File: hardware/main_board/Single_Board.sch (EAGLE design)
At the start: 54 parts, among them J2 U.FL, J3 AVR_SPI_PROG_3X2NS, Q1 2N7002, Q2 AO3400A, Q3 S9015, U1 INA199B1DCKR, U2 MCP1703T-3302E/CB, U4 W25X40CLUXIG_TR, U5 ATMEGA328PB-AU, X1 32.768KHZ-FC-135, X2 B2B-PH-K-S, X3 B2B-XH-2, X4 BM02B-SRSS-TB, X5 BM02B-SRSS-TB

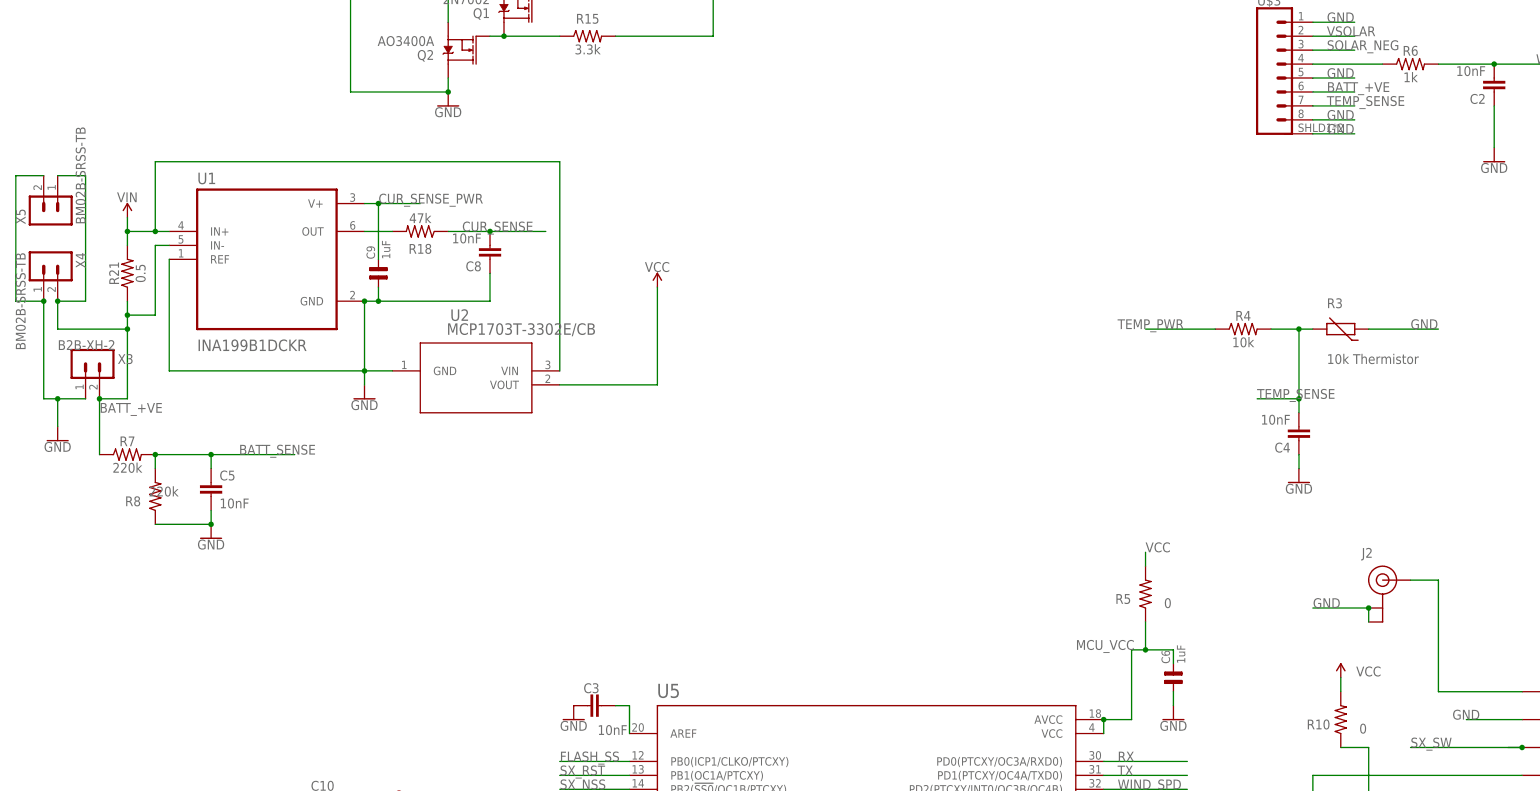
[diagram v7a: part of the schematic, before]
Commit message: Board improvements: Fixed 8P8C jack footprint. Better antenna trace impedance. Added anti-static resistor to antenna
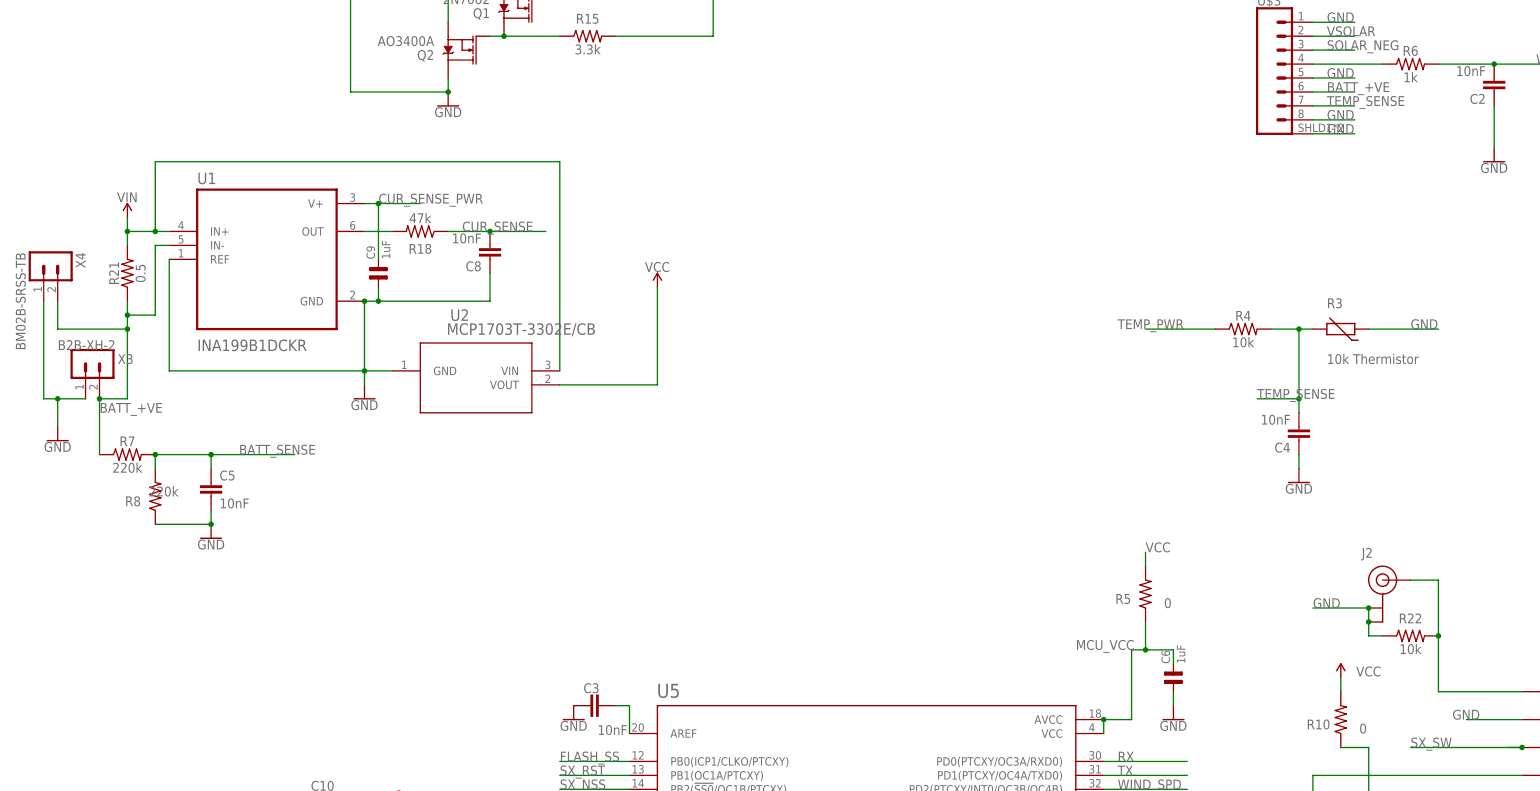
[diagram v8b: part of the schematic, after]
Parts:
- removed X5: BM02B-SRSS-TB, main_board:BM02B-SRSS-TB
- added R22: 10k, SparkFun-Resistors:RESISTOR0805
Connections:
- net ANT: now also R22.2
- net BATT_+VE: no longer X5.1
- net GND: now also R22.1; no longer X5.2
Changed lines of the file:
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@@
 <grid distance="0.1" unitdist="inch" unit="inch" style="lines" multiple="1" display="no" altdistance="0.01" altunitdist="inch" altunit="inch"/>
 <layers>
-<layer number="1" name="Top" color="4" fill="1" visible="yes" active="no"/>
-<layer number="16" name="Bottom" color="1" fill="1" visible="yes" active="no"/>
-<layer number="17" name="Pads" color="2" fill="1" visible="yes" active="no"/>
-<layer number="18" name="Vias" color="2" fill="1" visible="yes" active="no"/>
-<layer number="19" name="Unrouted" color="6" fill="1" visible="yes" active="no"/>
-<layer number="20" name="Dimension" color="36" fill="1" visible="yes" active="no"/>
-<layer number="21" name="tPlace" color="7" fill="1" visible="yes" active="no"/>
-<layer number="22" name="bPlace" color="7" fill="1" visible="yes" active="no"/>
-<layer number="23" name="tOrigins" color="15" fill="1" visible="yes" active="no"/>
-<layer number="24" name="bOrigins" color="15" fill="1" visible="yes" active="no"/>
-<layer number="25" name="tNames" color="7" fill="1" visible="yes" active="no"/>
-<layer number="26" name="bNames" color="7" fill="1" visible="yes" active="no"/>
-<layer number="27" name="tValues" color="7" fill="1" visible="yes" active="no"/>
-<layer number="28" name="bValues" color="7" fill="1" visible="yes" active="no"/>
+<layer number="1" name="Top" color="4" fill="1" visible="no" active="no"/>
+<layer number="16" name="Bottom" color="1" fill="1" visible="no" active="no"/>
+<layer number="17" name="Pads" color="2" fill="1" visible="no" active="no"/>
+<layer number="18" name="Vias" color="2" fill="1" visible="no" active="no"/>
+<layer number="19" name="Unrouted" color="6" fill="1" visible="no" active="no"/>
+<layer number="20" name="Dimension" color="36" fill="1" visible="no" active="no"/>
+<layer number="21" name="tPlace" color="7" fill="1" visible="no" active="no"/>
+<layer number="22" name="bPlace" color="7" fill="1" visible="no" active="no"/>
+<layer number="23" name="tOrigins" color="15" fill="1" visible="no" active="no"/>
+<layer number="24" name="bOrigins" color="15" fill="1" visible="no" active="no"/>
+<layer number="25" name="tNames" color="7" fill="1" visible="no" active="no"/>
+<layer number="26" name="bNames" color="7" fill="1" visible="no" active="no"/>
+<layer number="27" name="tValues" color="7" fill="1" visible="no" active="no"/>
+<layer number="28" name="bValues" color="7" fill="1" visible="no" active="no"/>
 <layer number="29" name="tStop" color="7" fill="3" visible="no" active="no"/>
 <layer number="30" name="bStop" color="7" fill="6" visible="no" active="no"/>
@@
 <layer number="35" name="tGlue" color="7" fill="4" visible="no" active="no"/>
 <layer number="36" name="bGlue" color="7" fill="5" visible="no" active="no"/>
-<layer number="37" name="tTest" color="7" fill="1" visible="yes" active="no"/>
-<layer number="38" name="bTest" color="7" fill="1" visible="yes" active="no"/>
+<layer number="37" name="tTest" color="7" fill="1" visible="no" active="no"/>
+<layer number="38" name="bTest" color="7" fill="1" visible="no" active="no"/>
 <layer number="39" name="tKeepout" color="4" fill="11" visible="no" active="no"/>
 <layer number="40" name="bKeepout" color="1" fill="11" visible="no" active="no"/>
@@
 <layer number="44" name="Drills" color="7" fill="1" visible="no" active="no"/>
 <layer number="45" name="Holes" color="7" fill="1" visible="no" active="no"/>
-<layer number="46" name="Milling" color="3" fill="1" visible="yes" active="no"/>
-<layer number="47" name="Measures" color="7" fill="1" visible="yes" active="no"/>
-<layer number="48" name="Document" color="7" fill="1" visible="yes" active="no"/>
-<layer number="49" name="Reference" color="7" fill="1" visible="yes" active="no"/>
-<layer number="50" name="dxf" color="7" fill="1" visible="yes" active="no"/>
-<layer number="51" name="tDocu" color="7" fill="1" visible="yes" active="no"/>
-<layer number="52" name="bDocu" color="7" fill="1" visible="yes" active="no"/>
-<layer number="53" name="tGND_GNDA" color="7" fill="9" visible="yes" active="no"/>
-<layer number="54" name="bGND_GNDA" color="1" fill="9" visible="yes" active="no"/>
-<layer number="56" name="wert" color="7" fill="1" visible="yes" active="no"/>
-<layer number="57" name="tCAD" color="7" fill="1" visible="yes" active="no"/>
-<layer number="59" name="tCarbon" color="7" fill="1" visible="yes" active="no"/>
-<layer number="60" name="bCarbon" color="7" fill="1" visible="yes" active="no"/>
+<layer number="46" name="Milling" color="3" fill="1" visible="no" active="no"/>
+<layer number="47" name="Measures" color="7" fill="1" visible="no" active="no"/>
+<layer number="48" name="Document" color="7" fill="1" visible="no" active="no"/>
+<layer number="49" name="Reference" color="7" fill="1" visible="no" active="no"/>
+<layer number="50" name="dxf" color="7" fill="1" visible="no" active="no"/>
+<layer number="51" name="tDocu" color="7" fill="1" visible="no" active="no"/>
+<layer number="52" name="bDocu" color="7" fill="1" visible="no" active="no"/>
+<layer number="53" name="tGND_GNDA" color="7" fill="9" visible="no" active="no"/>
+<layer number="54" name="bGND_GNDA" color="1" fill="9" visible="no" active="no"/>
+<layer number="56" name="wert" color="7" fill="1" visible="no" active="no"/>
+<layer number="57" name="tCAD" color="7" fill="1" visible="no" active="no"/>
+<layer number="59" name="tCarbon" color="7" fill="1" visible="no" active="no"/>
+<layer number="60" name="bCarbon" color="7" fill="1" visible="no" active="no"/>
 <layer number="88" name="SimResults" color="9" fill="1" visible="yes" active="yes"/>
 <layer number="89" name="SimProbes" color="9" fill="1" visible="yes" active="yes"/>
@@
 <part name="U4" library="main_board" deviceset="W25X40CLUXIG_TR" device=""/>
 <part name="X4" library="main_board" deviceset="BM02B-SRSS" device="-TB"/>
-<part name="X5" library="main_board" deviceset="BM02B-SRSS" device="-TB"/>
 <part name="R20" library="SparkFun-Resistors" library_urn="urn:adsk.eagle:library:532" deviceset="RESISTOR" device="0805" package3d_urn="urn:adsk.eagle:package:39651/1" value="10k"/>
+<part name="R22" library="SparkFun-Resistors" library_urn="urn:adsk.eagle:library:532" deviceset="RESISTOR" device="0805" package3d_urn="urn:adsk.eagle:package:39651/1" value="10k"/>
 </parts>
 <sheets>
@@
 <attribute name="NAME" x="-136.398" y="-13.97" size="1.778" layer="95" rot="R270"/>
 </instance>
-<instance part="X5" gate="G$1" x="-142.24" y="-7.62" smashed="yes" rot="R90">
-<attribute name="VALUE" x="-134.62" y="-8.89" size="1.778" layer="96" rot="R90"/>
-<attribute name="NAME" x="-145.542" y="-8.89" size="1.778" layer="95" rot="R90"/>
-</instance>
 <instance part="R20" gate="G$1" x="-33.02" y="40.64" smashed="yes">
 <attribute name="NAME" x="-33.02" y="44.704" size="1.778" layer="95" font="vector" rot="R180" align="bottom-center"/>
 <attribute name="VALUE" x="-33.02" y="39.116" size="1.778" layer="96" font="vector" align="top-center"/>
+</instance>
+<instance part="R22" gate="G$1" x="106.68" y="-83.82" smashed="yes">
+<attribute name="NAME" x="106.68" y="-79.756" size="1.778" layer="95" font="vector" rot="R180" align="bottom-center"/>
+<attribute name="VALUE" x="106.68" y="-85.344" size="1.778" layer="96" font="vector" align="top-center"/>
 </instance>
 </instances>
@@
 <wire x1="-142.24" y1="-40.64" x2="-139.7" y2="-40.64" width="0.1524" layer="91"/>
 <junction x="-139.7" y="-40.64"/>
-<wire x1="-142.24" y1="-22.86" x2="-147.32" y2="-22.86" width="0.1524" layer="91"/>
-<junction x="-142.24" y="-22.86"/>
-<wire x1="-147.32" y1="-22.86" x2="-147.32" y2="0" width="0.1524" layer="91"/>
-<pinref part="X5" gate="G$1" pin="2"/>
-<wire x1="-147.32" y1="0" x2="-142.24" y2="0" width="0.1524" layer="91"/>
 </segment>
 <segment>
@@
 <junction x="99.06" y="-78.74"/>
 <label x="88.9" y="-78.74" size="1.778" layer="95"/>
+<pinref part="R22" gate="G$1" pin="1"/>
+<wire x1="101.6" y1="-83.82" x2="99.06" y2="-83.82" width="0.1524" layer="91"/>
+<wire x1="99.06" y1="-83.82" x2="99.06" y2="-81.28" width="0.1524" layer="91"/>
+<junction x="99.06" y="-81.28"/>
 </segment>
 <segment>
@@
 <net name="ANT" class="0">
 <segment>
-<wire x1="111.76" y1="-93.98" x2="111.76" y2="-73.66" width="0.1524" layer="91"/>
+<wire x1="111.76" y1="-93.98" x2="111.76" y2="-83.82" width="0.1524" layer="91"/>
 <pinref part="U$2" gate="G$1" pin="ANT"/>
+<wire x1="111.76" y1="-83.82" x2="111.76" y2="-73.66" width="0.1524" layer="91"/>
 <wire x1="127" y1="-93.98" x2="111.76" y2="-93.98" width="0.1524" layer="91"/>
 <pinref part="J2" gate="G$1" pin="SIGNAL"/>
 <wire x1="106.68" y1="-73.66" x2="111.76" y2="-73.66" width="0.1524" layer="91"/>
+<pinref part="R22" gate="G$1" pin="2"/>
+<junction x="111.76" y="-83.82"/>
 </segment>
 </net>
@@
 <wire x1="-139.7" y1="-27.94" x2="-127" y2="-27.94" width="0.1524" layer="91"/>
 <junction x="-127" y="-27.94"/>
-<pinref part="X5" gate="G$1" pin="1"/>
-<wire x1="-139.7" y1="0" x2="-134.62" y2="0" width="0.1524" layer="91"/>
-<wire x1="-134.62" y1="0" x2="-134.62" y2="-22.86" width="0.1524" layer="91"/>
-<wire x1="-134.62" y1="-22.86" x2="-139.7" y2="-22.86" width="0.1524" layer="91"/>
-<junction x="-139.7" y="-22.86"/>
-</segment>
-<segment>
+</segment>
+<segment>
